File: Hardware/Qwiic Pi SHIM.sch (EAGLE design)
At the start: 12 parts, among them J1 Qwiic Right Angle, U2 3.3V/600mA

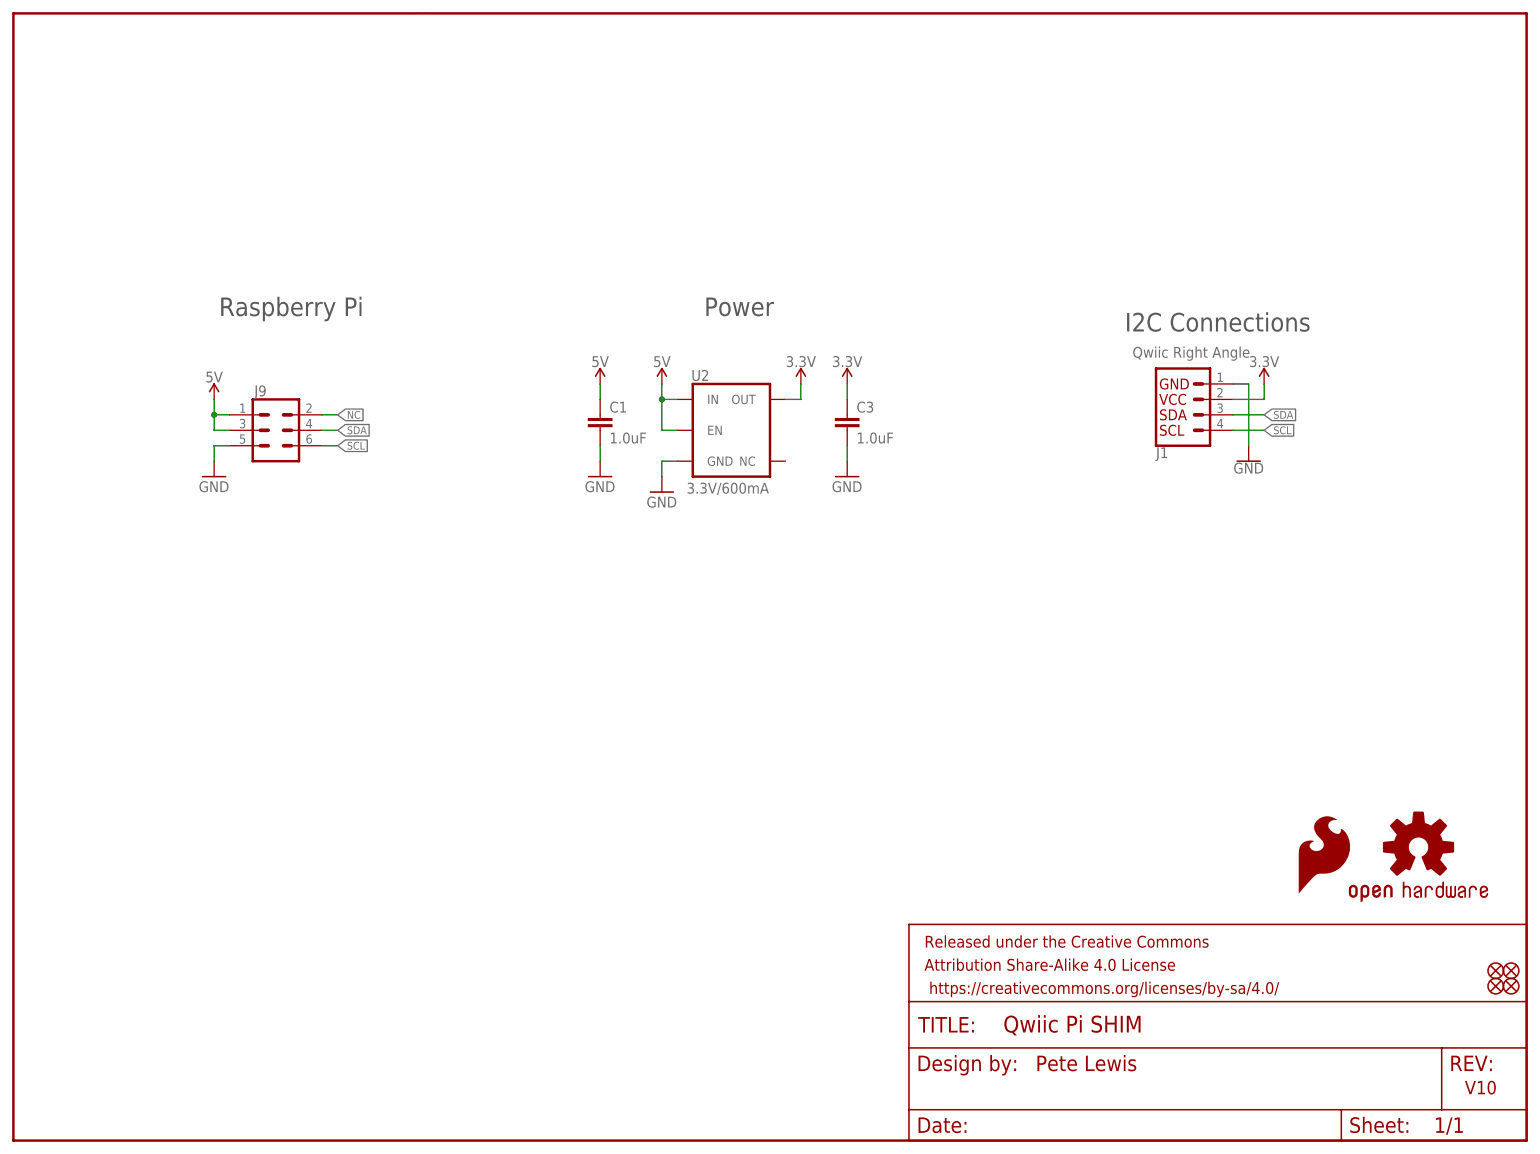
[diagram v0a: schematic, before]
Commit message: fixed orientation so it goes over the pi
added ordering instructions - 0.8mm thickness
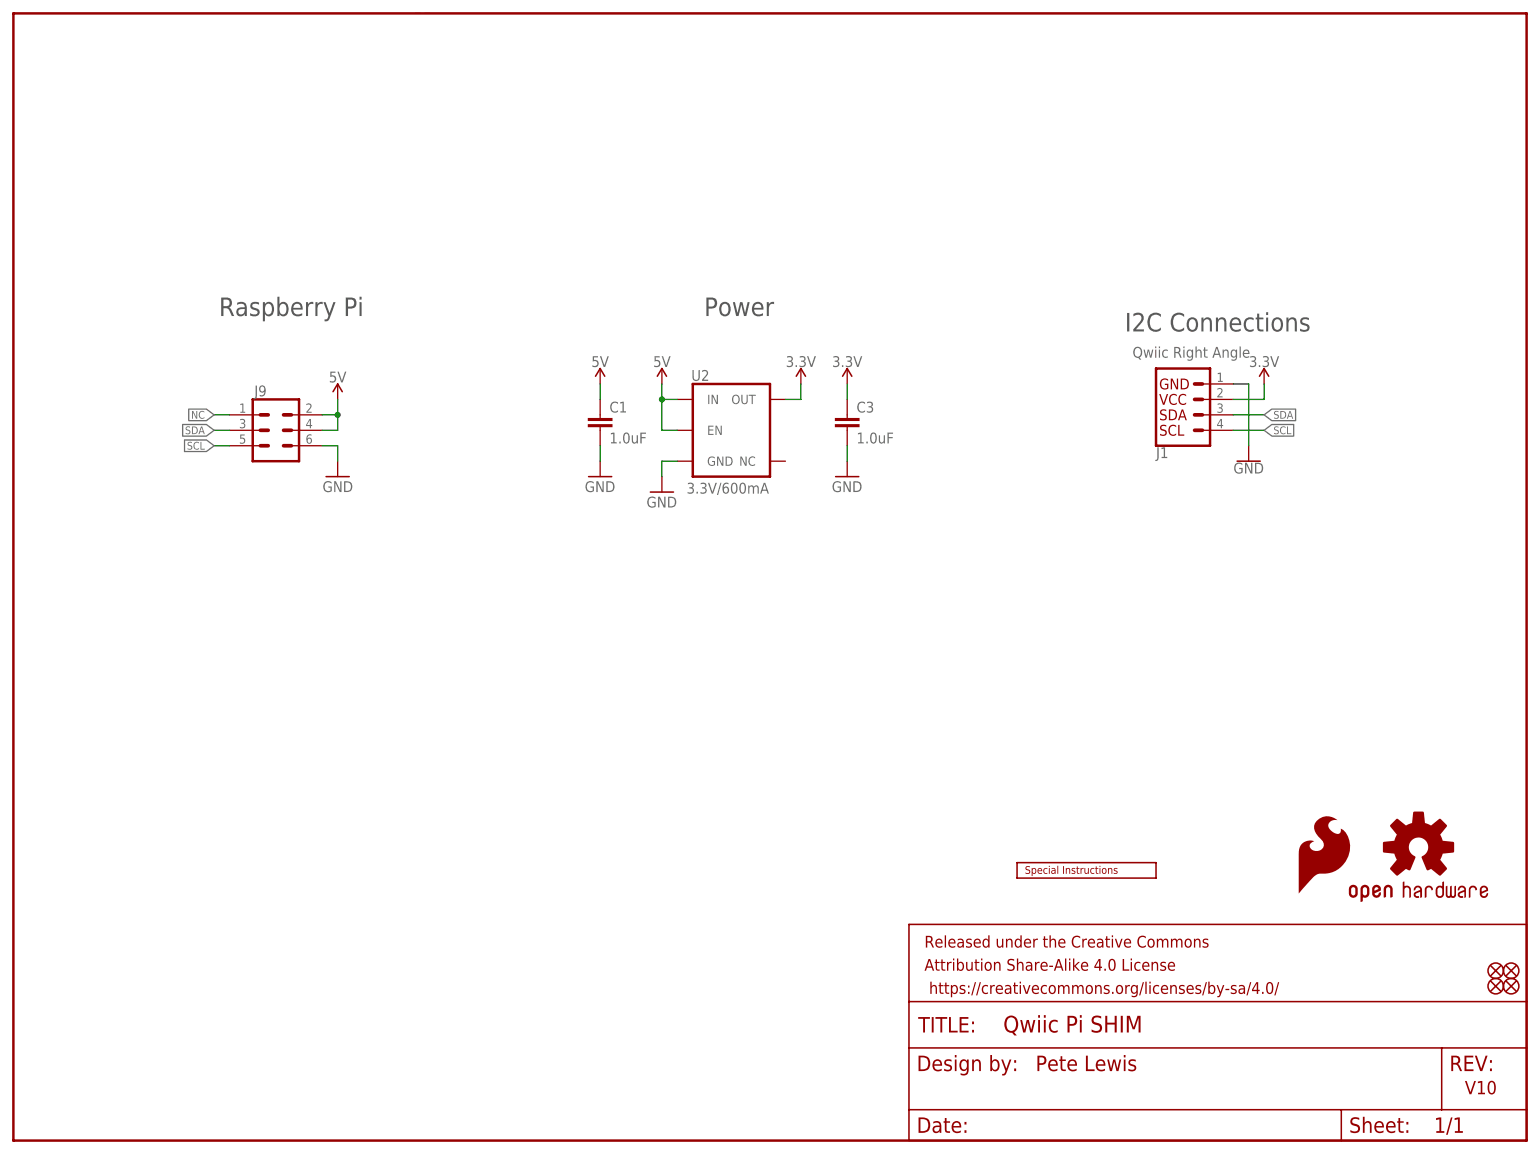
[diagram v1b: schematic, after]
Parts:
- added U$4: SPECIAL_INSTRUCTIONS-ORDERING, SparkFun-Aesthetics:SPECIAL_INSTRUCTIONS-ORDERING
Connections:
- net 5V: now also J9.2, J9.4; no longer J9.1, J9.3
- net GND: now also J9.6; no longer J9.5
- net NC: now also J9.1; no longer J9.2
- net SCL: now also J9.5; no longer J9.6
- net SDA: now also J9.3; no longer J9.4

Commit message: Single slot version done
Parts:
- J9: device SparkFun-Connectors:CONN_03X2NO_SILK -> Qwiic Pi SHIM:SPARKFUN-CONNECTORS_CONN_03X2PISHIM_LOCK_SLOTS
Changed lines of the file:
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@@
 <part name="FD3" library="SparkFun-Aesthetics" deviceset="FIDUCIAL" device="UFIDUCIAL" value="FIDUCIALUFIDUCIAL"/>
 <part name="FD4" library="SparkFun-Aesthetics" deviceset="FIDUCIAL" device="UFIDUCIAL" value="FIDUCIALUFIDUCIAL"/>
-<part name="J9" library="SparkFun-Connectors" deviceset="CONN_03X2" device="NO_SILK"/>
+<part name="J9" library="Qwiic Pi SHIM" deviceset="SPARKFUN-CONNECTORS_CONN_03X2" device="PISHIM_LOCK_SLOTS"/>
 <part name="SUPPLY6" library="SparkFun-PowerSymbols" deviceset="5V" device=""/>
 <part name="GND1" library="SparkFun" deviceset="GND" device=""/>
